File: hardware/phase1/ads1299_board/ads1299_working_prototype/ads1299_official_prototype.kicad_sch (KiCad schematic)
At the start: 139 parts, among them J2 1725656, J3 Conn_02x10_Odd_Even, J6 36PIN_IDC, J9 1725656, U1 ADS1299IPAG, U10 24AA256-I/ST, U4 OPA376, U5 TPS60403DBVT, U6 TPS73225DBVT, U7 TPS72325DBVT

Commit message: Schematic and PCB Update, new folder for updates in working prototype
ads1299 working prototype has folder for updated schematic and PCB now. Schematic update with J3 proper symbol, layout removing the unipolar power portions.
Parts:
- removed C68, C71: 100uF, LMK325BJ107MM_T:CAPC3225X280N, symbol Device:C_Small
- removed C69, C70: 0.1uF, GRM188R71H104KA93D:CAPC1608X90N, symbol Device:C_Small
- removed J3: Conn_02x10_Odd_Even, TSM-110-01-T-DV-P-TR:SAMTEC_TSM-110-01-T-DV-P-TR, symbol Connector_Generic:Conn_02x10_Odd_Even
- removed J4, J5: ~, SSW-105-22-F-D-VS-K:SAMTEC_SSW-105-22-F-D-VS-K, symbol Connector_Generic:Conn_02x05_Odd_Even
- removed JP24: TSW-103-07-T-S, TSW-103-07-T-S:SAMTEC_TSW-103-07-T-S, symbol TSW-103-07-T-S:TSW-103-07-T-S
- removed JP4: TSW-102-07-T-S, TSW-102-07-T-S:SAMTEC_TSW-102-07-T-S, symbol TSW-102-07-T-S:TSW-102-07-T-S
- removed R74: 0, RC0402JR-070RL:RESC1005X40, symbol Device:R_Small
- removed TP10, TP7, TP9: 5001, 5000:KEYSTONE_5000, symbol 5001:5001
- removed TP8: 5001, 5001:KEYSTONE_5001, symbol 5001:5001
- added J1, J7: Conn_02x16_Odd_Even, symbol Connector_Generic:Conn_02x16_Odd_Even
- added J3: TSM-110-01-T-DV-P-TR, TSM-110-01-T-DV-P-TR:SAMTEC_TSM-110-01-T-DV-P-TR, symbol TSM-110-01-T-DV-P-TR:TSM-110-01-T-DV-P-TR
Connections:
- net AVDD: now also J1.19 (Pin_19), J1.21 (Pin_21), J1.22 (Pin_22), J7.22 (Pin_22), J7.24 (Pin_24), J7.27 (Pin_27)
- net AVSS: now also J1.20 (Pin_20), J1.23 (Pin_23), J1.25 (Pin_25), J1.32 (Pin_32), J7.21 (Pin_21), J7.25 (Pin_25), J7.26 (Pin_26)
- net CLK: now also J7.5 (Pin_5)
- net CLKSEL: now also J7.20 (Pin_20)
- net DAISY_IN: now also J7.9 (Pin_9)
- net DVDD: now also J7.16 (Pin_16), J7.18 (Pin_18)
- net EXT_CLK: now also J3.17
- net GNDA: now also J1.31 (Pin_31), J3.04, J3.10, J3.18, J7.1 (Pin_1), J7.17 (Pin_17), J7.19 (Pin_19), J7.32 (Pin_32)
- net GPIO1: now also J3.06, J7.10 (Pin_10)
- net GPIO2: now also J3.12, J7.12 (Pin_12)
- net GPIO3: now also J7.13 (Pin_13)
- net GPIO4: now also J7.14 (Pin_14)
- net SCL: now also J3.16
- net SDA: now also J3.20
- net SPI_CLK: now also J3.03, J7.8 (Pin_8)
- net SPI_CS: now also J7.7 (Pin_7)
- net SPI_DRDY: now also J3.15, J7.15 (Pin_15)
- net SPI_IN: now also J3.11, J7.2 (Pin_2)
- net SPI_OUT: now also J3.13, J7.11 (Pin_11)
- net SPI_START: now also J7.6 (Pin_6)
- net VCAP1: now also J1.28 (Pin_28)
- net VCAP2: now also J1.30 (Pin_30)
- net VCAP3: now also J7.23 (Pin_23)
- net VCAP4: now also J1.26 (Pin_26)
- net VREFP: now also J1.24 (Pin_24)
- net /PWDN: now also J7.3 (Pin_3)
- net /RESET: now also J3.08, J7.4 (Pin_4)
- net at JP23.03: now also J3.02
- net at JP22.01: now also J3.14
- net at JP21.03, JP22.03: now also J3.01
- net at JP21.01: now also J3.07
- no-connect marks 23 -> 36
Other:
- moved on the sheet: AIN1, C1, C10, C11, C12, C13, C14, C15, C16, C17, C18, C19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

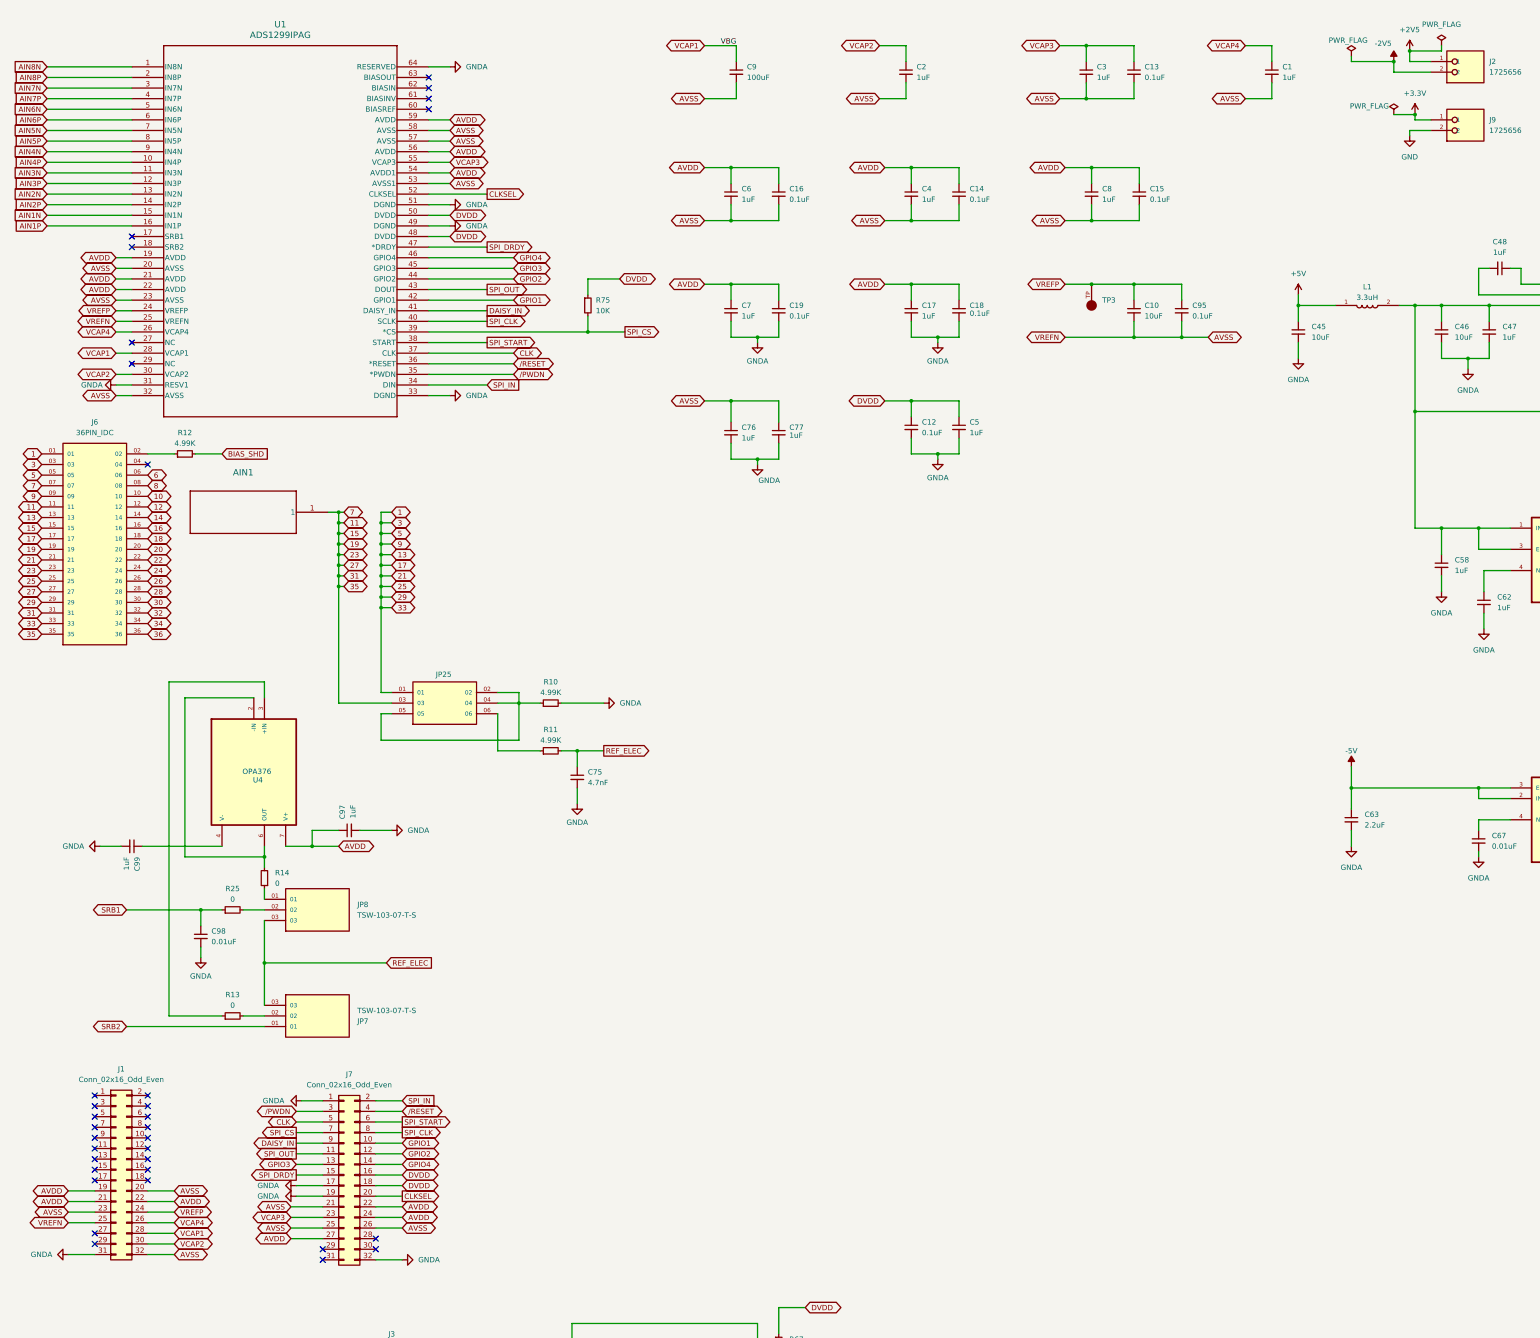
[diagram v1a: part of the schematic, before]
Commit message: Schematic and Layout updates
Added Bias stuff, routing now and updates from Schematic to Layout working beautifully now. trying to figure out if the capacitors are currently hooked up correctly for AVSS and AVDD or if we need more, not sure if the eval is following a unipolar or bipolar setup
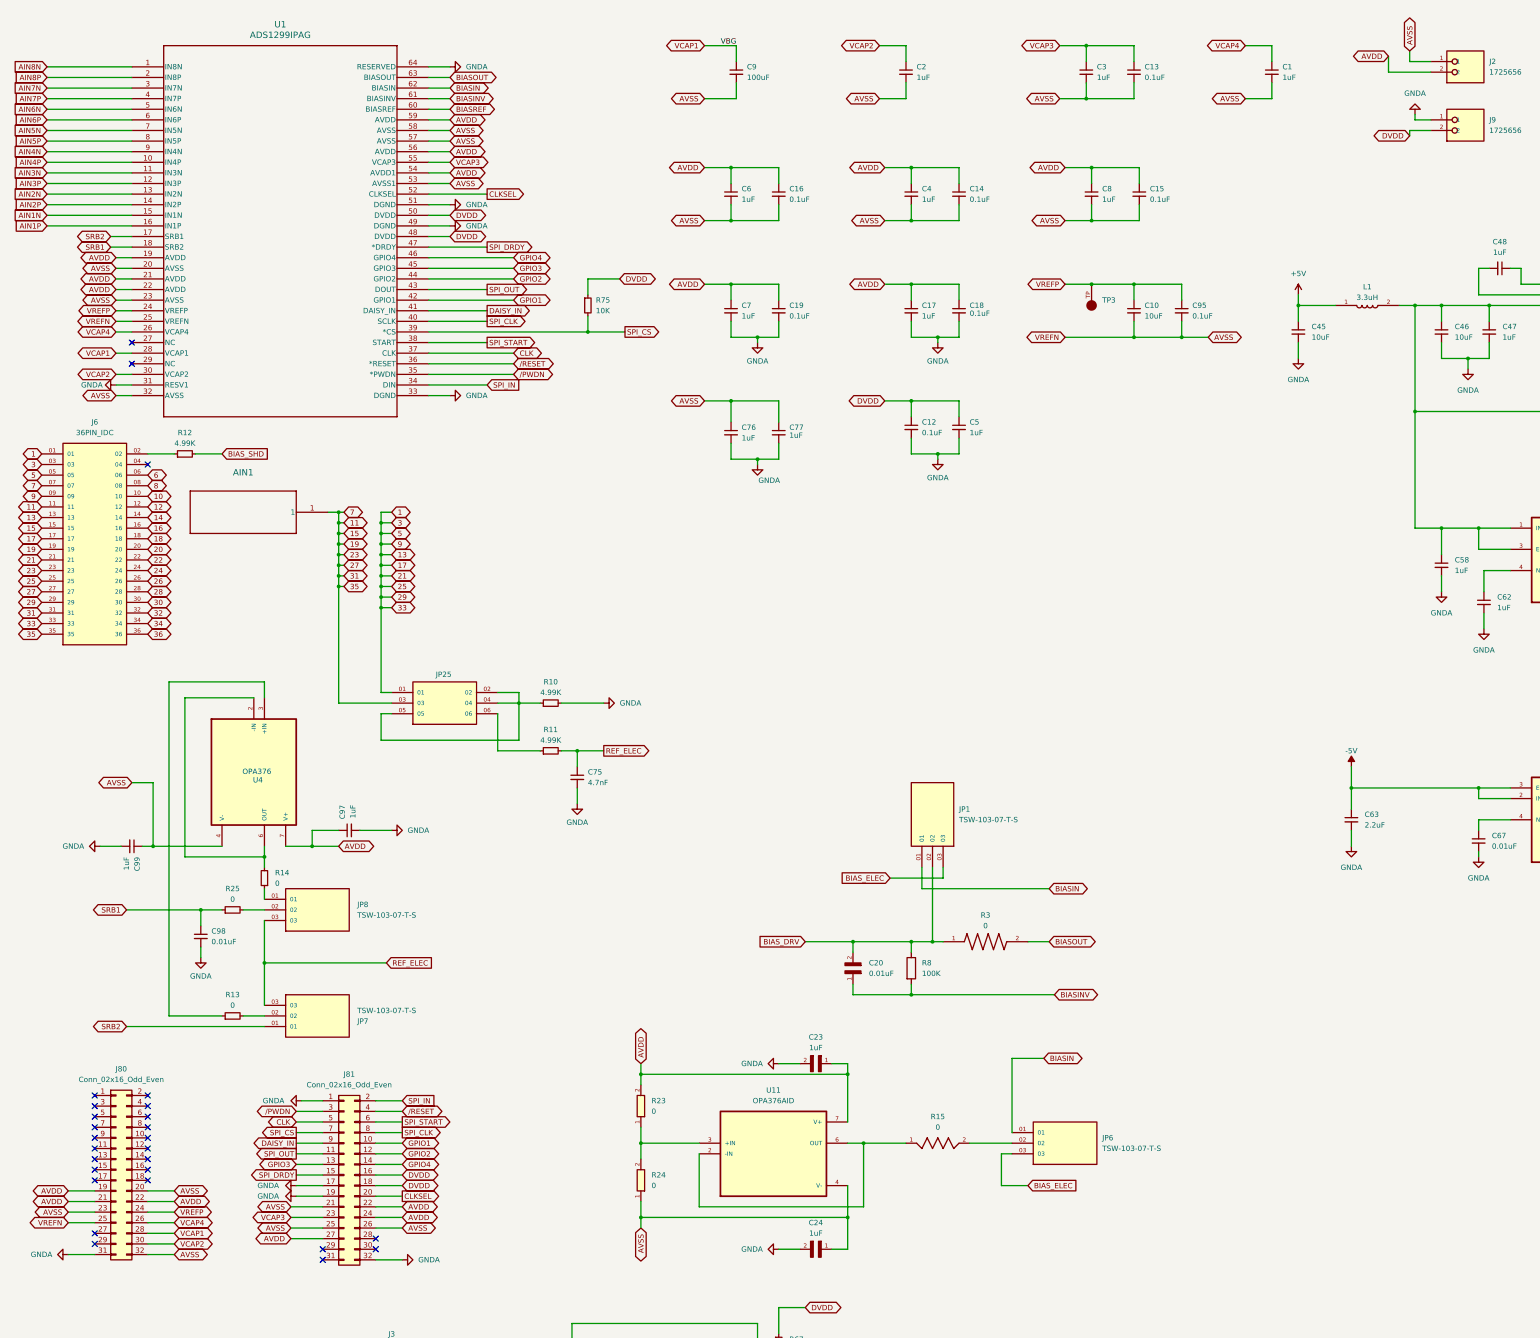
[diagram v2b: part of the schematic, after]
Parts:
- added C20: 0.01uF, GRM188R71H103KA01D:CAPC1608X90N, symbol GRM188R71H103KA01D:GRM188R71H103KA01D
- added C23, C24: 1uF, GRM188R61E105KA12D:CAPC1608X90N, symbol GRM188R61E105KA12D:GRM188R61E105KA12D
- added JP1, JP6: TSW-103-07-T-S, TSW-103-07-T-S:SAMTEC_TSW-103-07-T-S, symbol TSW-103-07-T-S:TSW-103-07-T-S
- added R15: 0, RC0402JR-070RL:RESC1005X40, symbol RC0402JR-070RL:RC0402JR-070RL
- added R23, R24: 0, RC0603JR-072ML:0603, symbol RC0603JR-072ML:RC0603JR-072ML
- added R3: 0, RC0603JR-070RL:RESC1607X60N, symbol RC0603JR-070RL:RC0603JR-070RL
- added R8: 100K, symbol Device:R
- added U11: OPA376AID, OPA376AID:SOIC127P599X175-8N, symbol OPA376AID:OPA376AID
- OSC1: footprint FXO-HC735:XTAL_FXO-HC735-8 -> FXO-HC735-8:XTAL_FXO-HC735-8
- TP1, TP11, TP12, TP13, TP2, TP4, TP5, TP6: MF Keystone Electronics Corp. -> Keystone Electronics
- renumbered J1 to J80, J7 to J81
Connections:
- net +2V5 is gone; now on net AVSS: J2.1
- net +3.3V is gone; now on net GNDA: J9.1
- net -2V5 is gone; now on net AVDD: J2.2
- net AVDD: now also C23.1, R23.2, U11.7 (V+)
- net AVSS: now also C99.1, U4.4 (V-), C24.1, R24.1, U11.4 (V-)
- net DVDD: now also J9.2
- net GND: no longer J9.2
- net GNDA: now also C23.2, C24.2
- net SRB1: now also U1.18 (SRB2)
- net SRB2: now also U1.17 (SRB1)
- net BIASREF: now reaches U1.60 (BIASREF)
- net BIASINV: now reaches U1.61 (BIASINV)
- net BIASINV: now also C20.1, R8.2
- net BIASIN: now reaches U1.62 (BIASIN)
- net BIASIN: now also JP1.01, JP6.01
- net BIASOUT: now reaches U1.63 (BIASOUT)
- net BIASOUT: now also R3.2
- new net: R15.1, U11.2 (-IN), U11.6 (OUT)
- new net: R23.1, R24.2, U11.3 (+IN)
- new net: JP6.02, R15.2
- new net BIAS_DRV: C20.2, JP1.02, R3.1, R8.1
- new net BIAS_ELEC: JP1.03, JP6.03
- no-connect marks 36 -> 30
